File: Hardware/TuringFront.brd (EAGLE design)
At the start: 107 x 49.5 mm, 73 parts, among them T1 2N3904, U1 TL074_

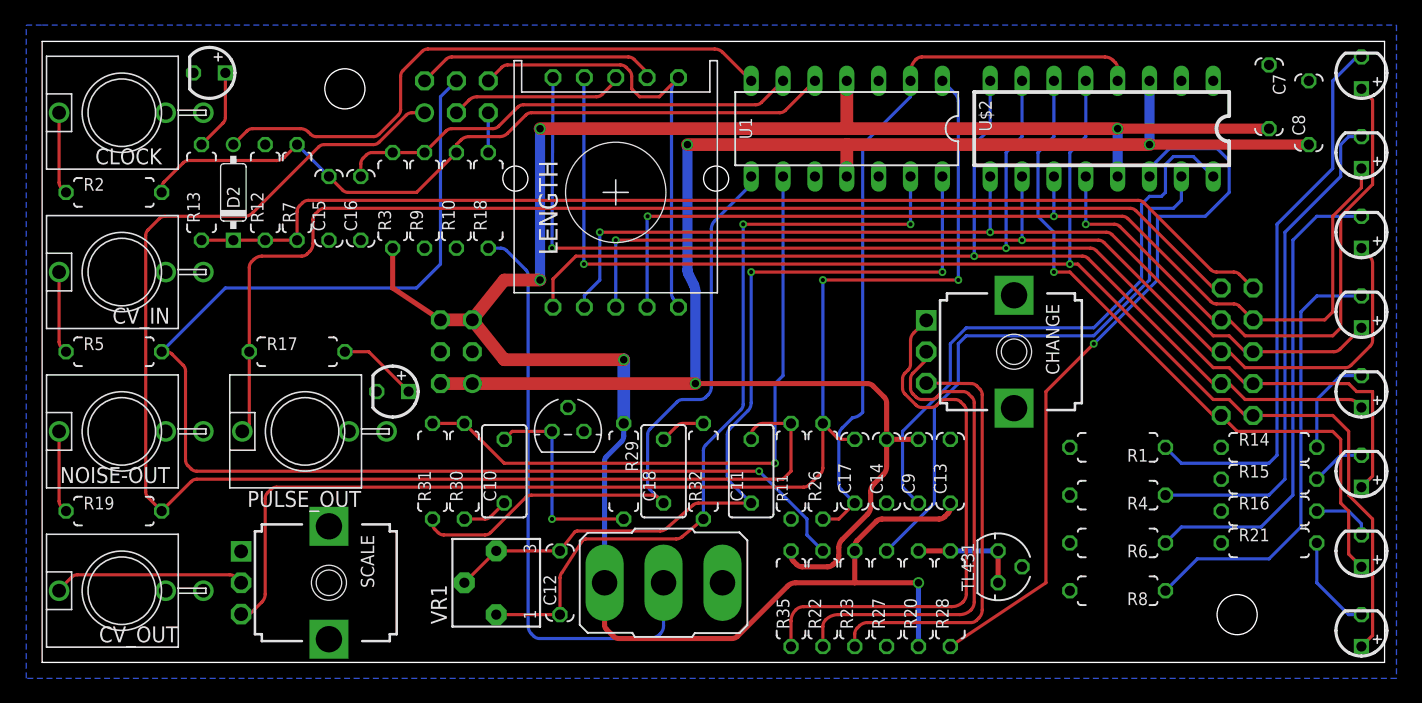
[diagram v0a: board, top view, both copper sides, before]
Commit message: minor rerouting
Fixes #22, fixes #21
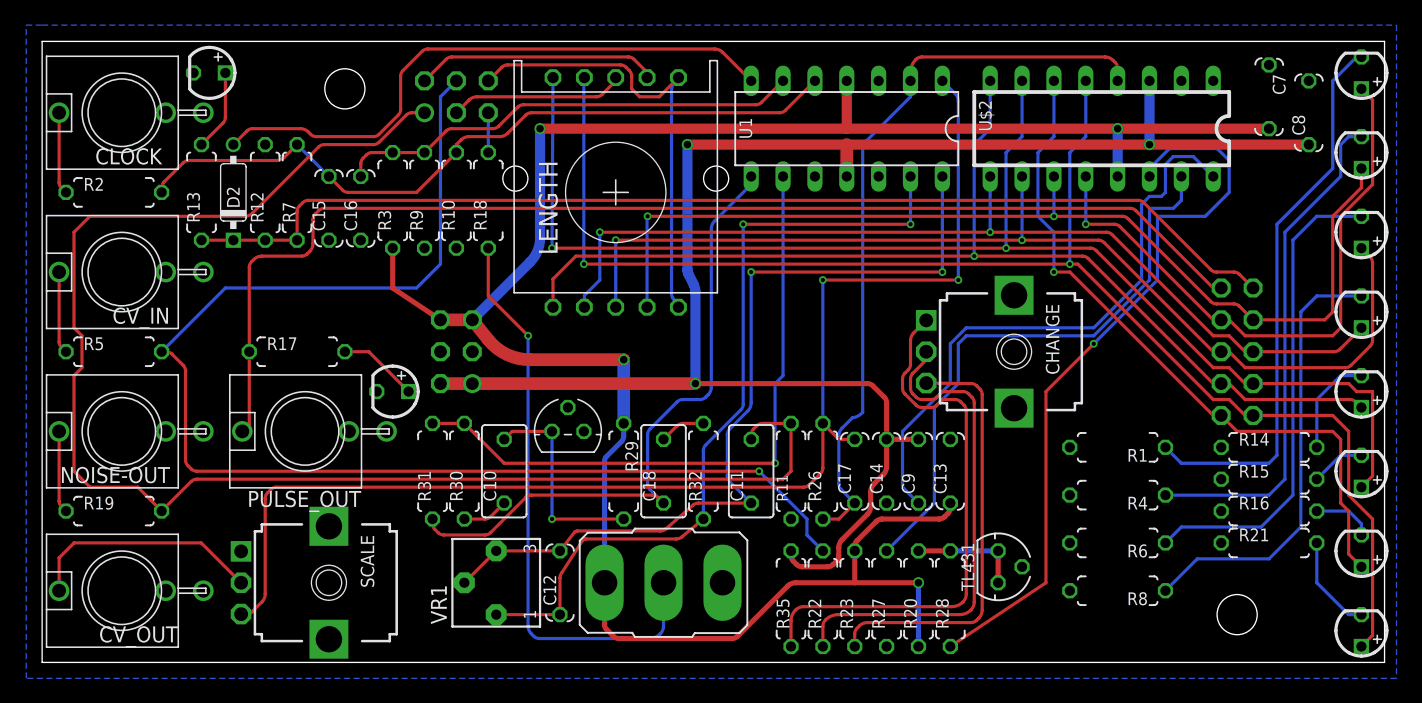
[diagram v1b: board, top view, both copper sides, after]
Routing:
- net NOISE_FRONT: track 107.9 -> 118.8 mm
- net N$39: track 15.3 -> 18.9 mm
- net +12V_FRONT: track 175.0 -> 172.9 mm, vias 5 -> 4
- net N$11: track 47.4 -> 46.7 mm, vias 0 -> 1
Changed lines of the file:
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@@
 </class>
 </classes>
-<designrules name="SeeedStudio_DRU_no_angle_20130527">
+<designrules name="SeeedStudio_DRU_no_angle_20130527 *">
 <description language="de">&lt;b&gt;EAGLE Design Rules&lt;/b&gt;
 &lt;p&gt;
@@
 <param name="mlMinCreamFrame" value="0mil"/>
 <param name="mlMaxCreamFrame" value="0mil"/>
-<param name="mlViaStopLimit" value="25mil"/>
+<param name="mlViaStopLimit" value="30mil"/>
 <param name="srRoundness" value="0"/>
 <param name="srMinRoundness" value="0mil"/>
@@
 <contactref element="FRONT_PWR" pad="5"/>
 <contactref element="U1" pad="4"/>
-<wire x1="34.29" y1="27.305" x2="36.83" y2="24.13" width="1.016" layer="1"/>
-<wire x1="36.83" y1="24.13" x2="46.355" y2="24.13" width="1.016" layer="1"/>
+<wire x1="34.29" y1="27.305" x2="35.551046875" y2="25.728690625" width="1.016" layer="1"/>
+<wire x1="35.551046875" y1="25.728690625" x2="38.877321875" y2="24.13" width="1.016" layer="1" curve="51.340205"/>
+<wire x1="38.877321875" y1="24.13" x2="46.355" y2="24.13" width="1.016" layer="1"/>
 <wire x1="46.355" y1="24.13" x2="46.355" y2="19.05" width="1.016" layer="16"/>
 <wire x1="34.29" y1="27.305" x2="31.75" y2="27.305" width="1.016" layer="1"/>
-<wire x1="85.725" y1="42.545" x2="64.135" y2="42.545" width="1.016" layer="1"/>
-<wire x1="64.135" y1="42.545" x2="39.6875" y2="42.545" width="1.016" layer="1"/>
-<wire x1="39.6875" y1="42.545" x2="39.6875" y2="30.48" width="0.8128" layer="16"/>
-<wire x1="39.6875" y1="30.48" x2="36.83" y2="30.48" width="1.016" layer="1"/>
-<wire x1="36.83" y1="30.48" x2="34.29" y2="27.305" width="1.016" layer="1"/>
-<via x="39.6875" y="42.545" extent="1-16" drill="0.6" shape="square"/>
-<via x="39.6875" y="30.48" extent="1-16" drill="0.6" shape="square"/>
-<via x="85.725" y="42.545" extent="1-16" drill="0.6" shape="square"/>
-<via x="46.355" y="24.13" extent="1-16" drill="0.6" shape="square"/>
-<wire x1="64.135" y1="46.355" x2="64.135" y2="42.545" width="1.016" layer="1"/>
+<wire x1="85.725" y1="42.545" x2="64.135" y2="42.545" width="0.8128" layer="1"/>
+<wire x1="64.135" y1="42.545" x2="39.6875" y2="42.545" width="0.8128" layer="1"/>
+<wire x1="39.6875" y1="42.545" x2="39.6875" y2="33.833815625" width="0.8128" layer="16"/>
+<wire x1="39.6875" y1="33.833815625" x2="38.8875375" y2="31.9025375" width="0.8128" layer="16" curve="-45.000046"/>
+<wire x1="38.8875375" y1="31.9025375" x2="34.29" y2="27.305" width="0.8128" layer="16"/>
+<via x="39.6875" y="42.545" extent="1-16" drill="0.6"/>
+<via x="85.725" y="42.545" extent="1-16" drill="0.6"/>
+<via x="46.355" y="24.13" extent="1-16" drill="0.6"/>
+<wire x1="64.135" y1="46.355" x2="64.135" y2="42.545" width="0.8128" layer="1"/>
 <wire x1="64.77" y1="8.89" x2="64.77" y2="6.35" width="0.4064" layer="1"/>
 <wire x1="44.831" y1="6.35" x2="44.831" y2="2.98366875" width="0.4064" layer="1"/>
@@
 <wire x1="22.0390125" y1="41.0890125" x2="16.773025" y2="35.823025" width="0.254" layer="1"/>
 <wire x1="16.773025" y1="35.823025" x2="16.138025" y2="35.56" width="0.254" layer="1" curve="-45"/>
-<wire x1="16.138025" y1="35.56" x2="9.788025" y2="35.56" width="0.254" layer="1"/>
-<wire x1="9.788025" y1="35.56" x2="9.3390125" y2="35.3740125" width="0.254" layer="1" curve="45"/>
-<wire x1="9.3390125" y1="35.3740125" x2="8.4409875" y2="34.4759875" width="0.254" layer="1"/>
-<wire x1="8.4409875" y1="34.4759875" x2="8.255" y2="34.026975" width="0.254" layer="1" curve="45"/>
-<wire x1="8.255" y1="34.026975" x2="8.255" y2="13.598025" width="0.254" layer="1"/>
-<wire x1="8.255" y1="13.598025" x2="8.4409875" y2="13.1490125" width="0.254" layer="1" curve="45"/>
-<wire x1="8.4409875" y1="13.1490125" x2="9.525" y2="12.065" width="0.254" layer="1"/>
+<wire x1="16.138025" y1="35.56" x2="3.81" y2="35.56" width="0.254" layer="1"/>
+<wire x1="3.81" y1="35.56" x2="2.54" y2="34.29" width="0.254" layer="1"/>
+<wire x1="2.54" y1="34.29" x2="2.54" y2="26.67" width="0.254" layer="1"/>
+<wire x1="2.54" y1="26.67" x2="3.175" y2="26.035" width="0.254" layer="1"/>
+<wire x1="3.175" y1="26.035" x2="3.175" y2="23.495" width="0.254" layer="1"/>
+<wire x1="3.175" y1="23.495" x2="2.54" y2="22.86" width="0.254" layer="1"/>
+<wire x1="2.54" y1="22.86" x2="2.54" y2="15.24" width="0.254" layer="1"/>
+<wire x1="2.54" y1="15.24" x2="3.81" y2="13.97" width="0.254" layer="1"/>
+<wire x1="3.81" y1="13.97" x2="7.62" y2="13.97" width="0.254" layer="1"/>
+<wire x1="7.62" y1="13.97" x2="9.525" y2="12.065" width="0.254" layer="1"/>
 </signal>
 <signal name="STEP_12_FRONT">
@@
 <contactref element="WRITE" pad="2"/>
 <contactref element="R18" pad="1"/>
-<wire x1="35.56" y1="33.02" x2="36.566975" y2="33.02" width="0.254" layer="16"/>
-<wire x1="36.566975" y1="33.02" x2="37.0159875" y2="32.8340125" width="0.254" layer="16" curve="-45"/>
-<wire x1="37.0159875" y1="32.8340125" x2="38.5490125" y2="31.3009875" width="0.254" layer="16"/>
-<wire x1="38.5490125" y1="31.3009875" x2="38.735" y2="30.851975" width="0.254" layer="16" curve="-45"/>
-<wire x1="38.735" y1="30.851975" x2="38.735" y2="2.911975" width="0.254" layer="16"/>
+<wire x1="38.735" y1="26.035" x2="38.735" y2="2.911975" width="0.254" layer="16"/>
 <wire x1="38.735" y1="2.911975" x2="38.998025" y2="2.276975" width="0.254" layer="16" curve="45"/>
 <wire x1="38.998025" y1="2.276975" x2="39.1840125" y2="2.0909875" width="0.254" layer="16"/>
@@
 <wire x1="49.266975" y1="2.276975" x2="49.53" y2="2.911975" width="0.254" layer="16" curve="45"/>
 <wire x1="49.53" y1="2.911975" x2="49.53" y2="6.35" width="0.254" layer="16"/>
+<via x="38.735" y="26.035" extent="1-16" drill="0.3302"/>
+<wire x1="38.735" y1="26.035" x2="35.56" y2="29.21" width="0.254" layer="1"/>
+<wire x1="35.56" y1="29.21" x2="35.56" y2="33.02" width="0.254" layer="1"/>
 </signal>
 <signal name="N$43">
@@
 <contactref element="CV_OUT" pad="P$1_TIP"/>
 <contactref element="SCALE" pad="2"/>
-<wire x1="1.35" y1="5.715" x2="1.35" y2="5.795" width="0.254" layer="1"/>
-<wire x1="1.35" y1="5.795" x2="2.3540125" y2="6.7990125" width="0.254" layer="1"/>
-<wire x1="2.3540125" y1="6.7990125" x2="2.803025" y2="6.985" width="0.254" layer="1" curve="-45"/>
-<wire x1="2.803025" y1="6.985" x2="14.961903125" y2="6.985" width="0.254" layer="1"/>
-<wire x1="14.961903125" y1="6.985" x2="15.4110375" y2="6.7989625" width="0.254" layer="1" curve="-44.999801"/>
-<wire x1="15.4110375" y1="6.7989625" x2="15.86" y2="6.35" width="0.254" layer="1"/>
+<wire x1="1.35" y1="5.715" x2="1.35" y2="8.335" width="0.254" layer="1"/>
+<wire x1="1.35" y1="8.335" x2="2.54" y2="9.525" width="0.254" layer="1"/>
+<wire x1="2.54" y1="9.525" x2="12.685" y2="9.525" width="0.254" layer="1"/>
+<wire x1="12.685" y1="9.525" x2="15.86" y2="6.35" width="0.254" layer="1"/>
 </signal>
 <signal name="N$40">
@@
 <wire x1="31.75" y1="22.225" x2="34.29" y2="22.225" width="1.016" layer="1"/>
 <wire x1="34.29" y1="22.225" x2="52.07" y2="22.225" width="1.016" layer="1"/>
-<wire x1="64.135" y1="41.275" x2="88.265" y2="41.275" width="1.016" layer="1"/>
-<via x="88.265" y="41.275" extent="1-16" drill="0.6" shape="square"/>
-<via x="52.07" y="22.225" extent="1-16" drill="0.6" shape="square"/>
+<wire x1="64.135" y1="41.275" x2="88.265" y2="41.275" width="0.8128" layer="1"/>
+<via x="88.265" y="41.275" extent="1-16" drill="0.6"/>
+<via x="52.07" y="22.225" extent="1-16" drill="0.6"/>
 <wire x1="52.07" y1="22.225" x2="65.776975" y2="22.225" width="0.4064" layer="1"/>
 <wire x1="65.776975" y1="22.225" x2="66.2259875" y2="22.0390125" width="0.4064" layer="1" curve="-45"/>
@@
 <wire x1="59.69" y1="8.518025" x2="59.69" y2="8.89" width="0.4064" layer="1"/>
 <wire x1="64.135" y1="38.735" x2="64.135" y2="41.275" width="1.016" layer="1"/>
-<wire x1="64.135" y1="41.275" x2="51.435" y2="41.275" width="1.016" layer="1"/>
+<wire x1="64.135" y1="41.275" x2="51.435" y2="41.275" width="0.8128" layer="1"/>
 <wire x1="51.435" y1="41.275" x2="51.435" y2="31.264903125" width="0.8128" layer="16"/>
 <wire x1="51.435" y1="31.264903125" x2="51.5020375" y2="30.980925" width="0.8128" layer="16" curve="26.564799"/>
@@
 <wire x1="51.935921875" y1="30.11315625" x2="52.07" y2="29.54519375" width="0.8128" layer="16" curve="-26.565114"/>
 <wire x1="52.07" y1="29.54519375" x2="52.07" y2="22.225" width="0.8128" layer="16"/>
-<via x="51.435" y="41.275" extent="1-16" drill="0.6" shape="square"/>
+<via x="51.435" y="41.275" extent="1-16" drill="0.6"/>
 <wire x1="88.265" y1="46.355" x2="88.265" y2="41.275" width="0.8128" layer="16"/>
 <wire x1="88.265" y1="41.275" x2="100.965" y2="41.275" width="0.8128" layer="1"/>

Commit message: Rev 4 Front and Back Boards complete
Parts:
- renumbered FRONT_BUS2 to LINK1, FRONT_PWR to LINK2, SV1 to LINK3
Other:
- board text added: "Music Thing Modular Turing Machine Rev 4 Front Board September 2015 CC-BY-SA"
- board text removed: "Music Thing Modular Turing Machine Rev 4 Prototype 1 Front Board September 2015 CC-BY-SA"

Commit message: Finalised V4 PCBs
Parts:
- moved R8 3.81 mm to (85.7, 9.53)
- moved R6 2.54 mm to (85.7, 12.1)
- moved R4 1.27 mm to (85.7, 14.6)
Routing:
- net N$31: track 40.5 -> 41.0 mm
- net N$33: track 35.4 -> 34.9 mm
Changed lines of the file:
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@@
 <layer number="19" name="Unrouted" color="6" fill="1" visible="no" active="yes"/>
 <layer number="20" name="Dimension" color="15" fill="1" visible="yes" active="yes"/>
-<layer number="21" name="tPlace" color="7" fill="1" visible="no" active="yes"/>
-<layer number="22" name="bPlace" color="7" fill="1" visible="yes" active="yes"/>
+<layer number="21" name="tPlace" color="7" fill="1" visible="yes" active="yes"/>
+<layer number="22" name="bPlace" color="7" fill="1" visible="no" active="yes"/>
 <layer number="23" name="tOrigins" color="15" fill="1" visible="yes" active="yes"/>
-<layer number="24" name="bOrigins" color="15" fill="1" visible="yes" active="yes"/>
-<layer number="25" name="tNames" color="7" fill="1" visible="no" active="yes"/>
-<layer number="26" name="bNames" color="7" fill="1" visible="yes" active="yes"/>
-<layer number="27" name="tValues" color="7" fill="1" visible="no" active="yes"/>
+<layer number="24" name="bOrigins" color="15" fill="1" visible="no" active="yes"/>
+<layer number="25" name="tNames" color="7" fill="1" visible="yes" active="yes"/>
+<layer number="26" name="bNames" color="7" fill="1" visible="no" active="yes"/>
+<layer number="27" name="tValues" color="7" fill="1" visible="yes" active="yes"/>
 <layer number="28" name="bValues" color="7" fill="1" visible="yes" active="yes"/>
 <layer number="29" name="tStop" color="7" fill="3" visible="no" active="yes"/>
@@
 <element name="SCALE" library="MusicThingModular" package="9MM_SNAP-IN_POT" value="50k" x="22.86" y="6.35" locked="yes" rot="R270"/>
 <element name="C17" library="TomW" package="C050-024X044" value="1n" x="64.77" y="15.24" rot="R90"/>
-<element name="TL431" library="TomW" package="TO92-CLP" value="" x="76.2" y="7.62" rot="R270"/>
+<element name="TL431" library="TomW" package="TO92-CLP" value="" x="76.2" y="7.62" smashed="yes" rot="R270">
+<attribute name="NAME" x="80.645" y="7.62" size="1.524" layer="25" ratio="10" rot="R270" align="top-center"/>
+</element>
 <element name="R20" library="TomW" package="0207/7" value="3.3k" x="69.85" y="5.08" rot="R90"/>
 <element name="C18" library="rcl" package="C050-035X075" value="0.47uf" x="49.53" y="15.24" rot="R90"/>
@@
 </element>
 <element name="R1" library="TomW" package="0207/7" value="2.2k" x="85.725" y="17.145" rot="R180"/>
-<element name="R4" library="TomW" package="0207/7" value="2.2k" x="85.725" y="13.335" rot="R180"/>
-<element name="R6" library="TomW" package="0207/7" value="2.2k" x="85.725" y="9.525" rot="R180"/>
-<element name="R8" library="TomW" package="0207/7" value="2.2k" x="85.725" y="5.715" rot="R180"/>
+<element name="R4" library="TomW" package="0207/7" value="2.2k" x="85.725" y="14.605" rot="R180"/>
+<element name="R6" library="TomW" package="0207/7" value="2.2k" x="85.725" y="12.065" rot="R180"/>
+<element name="R8" library="TomW" package="0207/7" value="2.2k" x="85.725" y="9.525" rot="R180"/>
 <element name="R14" library="TomW" package="0207/7" value="2.2k" x="97.79" y="17.145"/>
 <element name="R15" library="TomW" package="0207/7" value="2.2k" x="97.79" y="14.605"/>
@@
 <wire x1="99.06" y1="34.29" x2="99.06" y2="14.605" width="0.254" layer="16"/>
 <wire x1="99.06" y1="14.605" x2="97.79" y2="13.335" width="0.254" layer="16"/>
-<wire x1="97.79" y1="13.335" x2="89.535" y2="13.335" width="0.254" layer="16"/>
+<wire x1="97.79" y1="13.335" x2="90.805" y2="13.335" width="0.254" layer="16"/>
+<wire x1="90.805" y1="13.335" x2="89.535" y2="14.605" width="0.254" layer="16"/>
 </signal>
 <signal name="N$32">
@@
 <wire x1="99.695" y1="13.335" x2="97.155" y2="10.795" width="0.254" layer="16"/>
 <wire x1="97.155" y1="10.795" x2="90.805" y2="10.795" width="0.254" layer="16"/>
-<wire x1="90.805" y1="10.795" x2="89.535" y2="9.525" width="0.254" layer="16"/>
+<wire x1="90.805" y1="10.795" x2="89.535" y2="12.065" width="0.254" layer="16"/>
 </signal>
 <signal name="N$33">
@@
 <wire x1="100.33" y1="27.94" x2="100.33" y2="10.795" width="0.254" layer="16"/>
 <wire x1="100.33" y1="10.795" x2="97.79" y2="8.255" width="0.254" layer="16"/>
-<wire x1="97.79" y1="8.255" x2="92.075" y2="8.255" width="0.254" layer="16"/>
-<wire x1="92.075" y1="8.255" x2="89.535" y2="5.715" width="0.254" layer="16"/>
+<wire x1="97.79" y1="8.255" x2="90.805" y2="8.255" width="0.254" layer="16"/>
+<wire x1="90.805" y1="8.255" x2="89.535" y2="9.525" width="0.254" layer="16"/>
 </signal>
 <signal name="N$34">
@@
 <contactref element="U1" pad="10"/>
 <contactref element="R9" pad="1"/>
-<contactref element="U1" pad="3"/>
 <contactref element="CV_OUT" pad="P$3_SLEEVE"/>
 <contactref element="R12" pad="2"/>
@@
 <vertex x="-1.27" y="50.8"/>
 </polygon>
+<contactref element="U1" pad="3"/>
+<wire x1="93.98" y1="12.065" x2="93.98" y2="9.525" width="0" layer="19" extent="1-1"/>
+<wire x1="93.98" y1="14.605" x2="93.98" y2="12.065" width="0" layer="19" extent="1-1"/>
+<wire x1="93.98" y1="17.145" x2="93.98" y2="14.605" width="0" layer="19" extent="1-1"/>
 </signal>
 <signal name="WRITE_SW_FRONT">

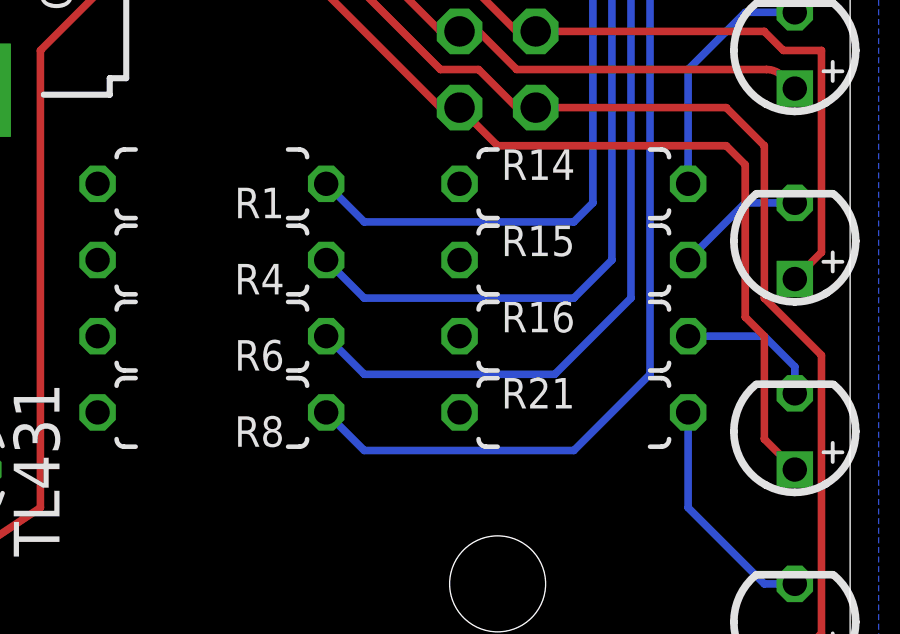
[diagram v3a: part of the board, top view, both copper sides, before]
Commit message: Update front board to fix error in ground plane
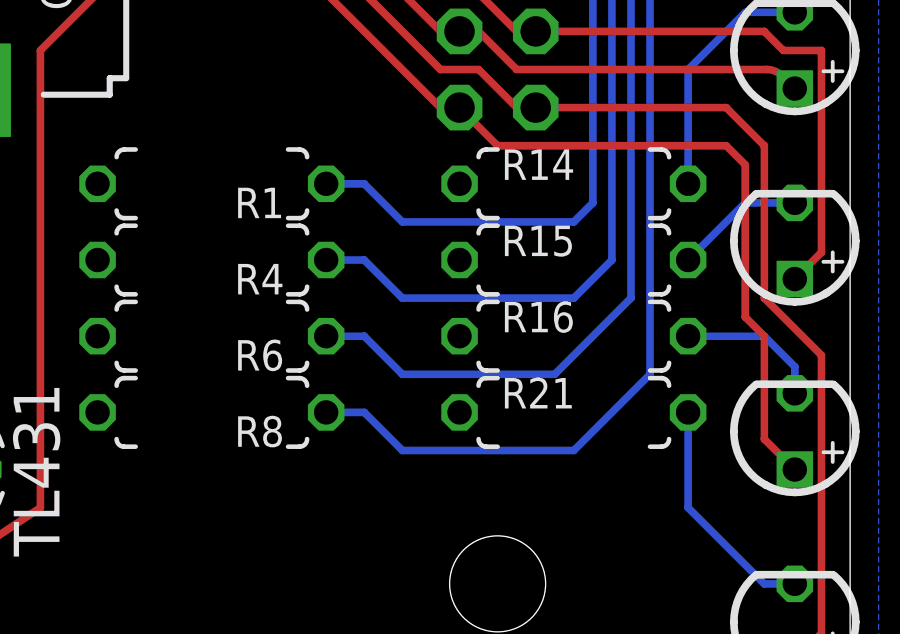
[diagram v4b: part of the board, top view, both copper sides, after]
